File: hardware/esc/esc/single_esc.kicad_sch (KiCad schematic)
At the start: 43 parts, among them Q1 Q_NMOS, Q2 Q_NMOS, Q3 Q_NMOS, Q4 Q_NMOS, Q5 Q_NMOS, Q6 Q_NMOS, U1 NSG2065Q, U2 AT32F421G8U7

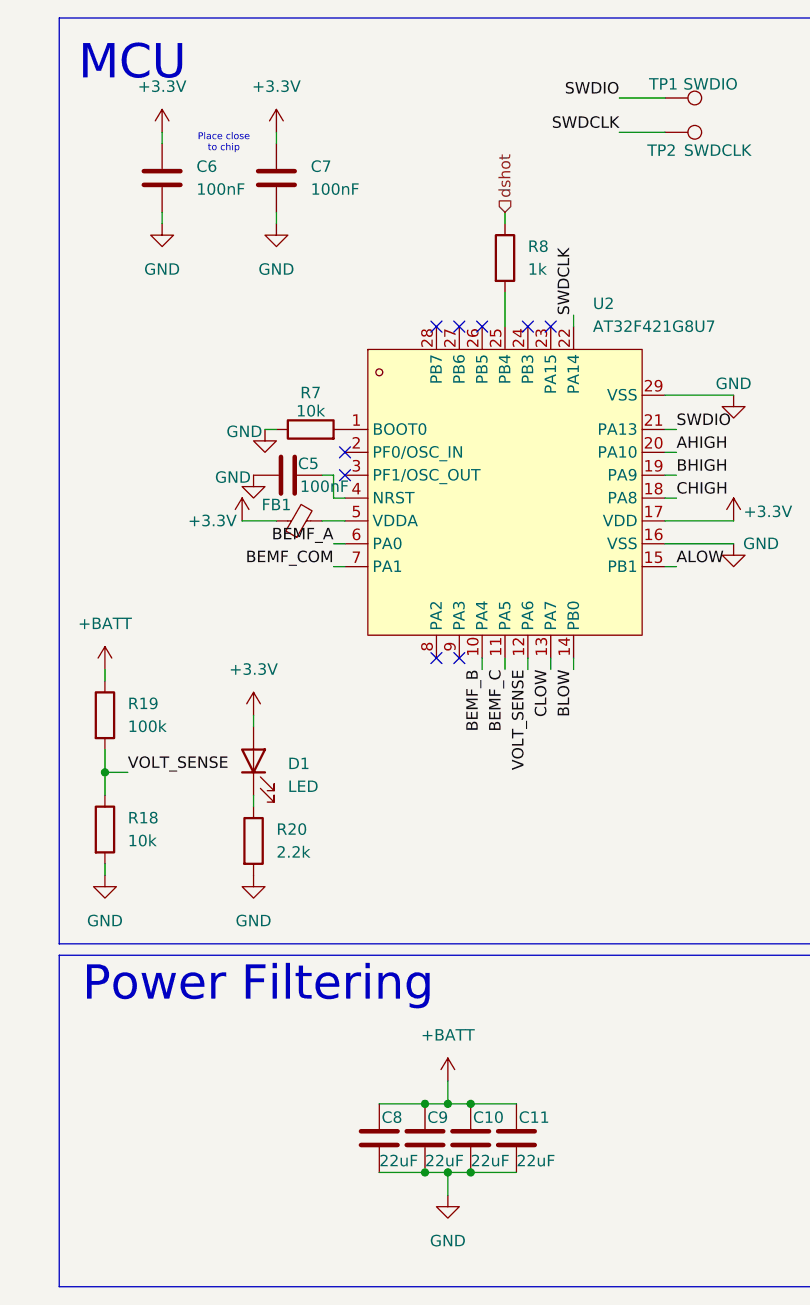
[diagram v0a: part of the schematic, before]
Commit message: redo layout and new board outline
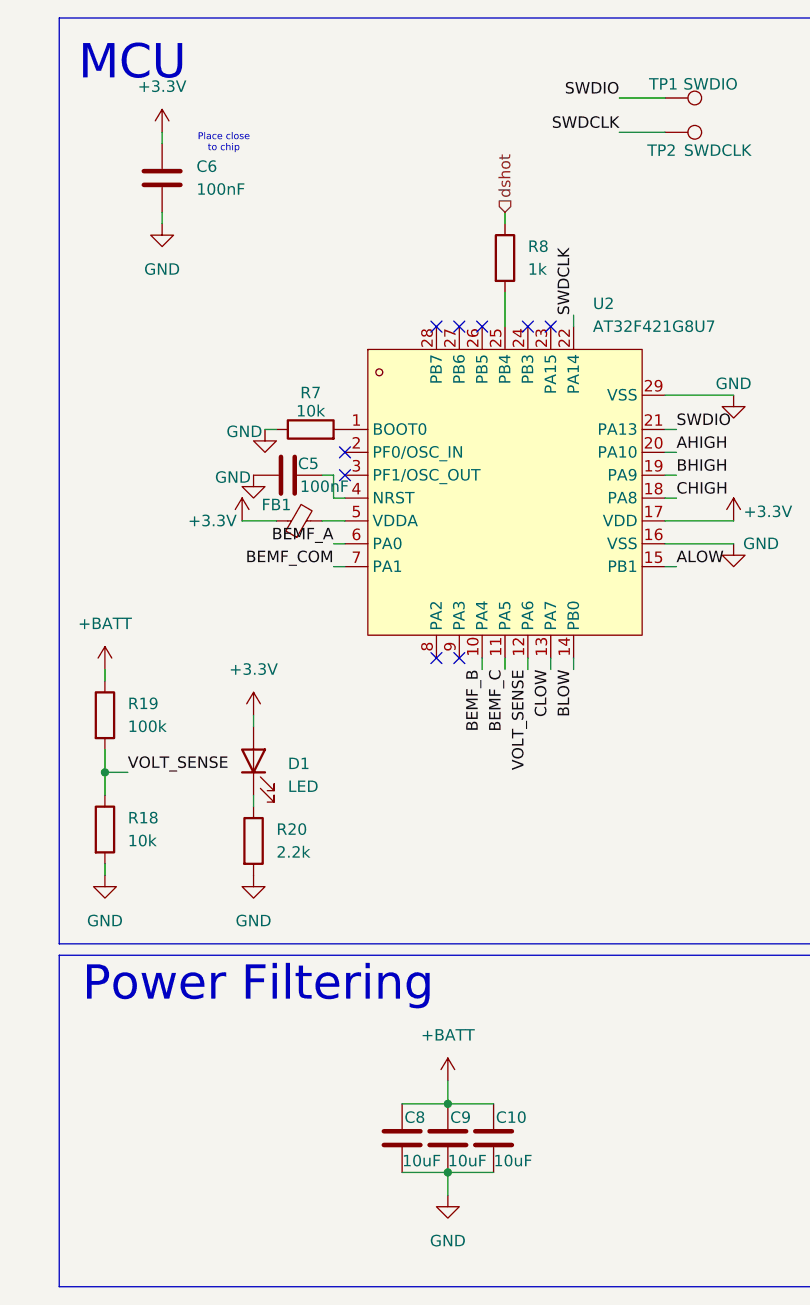
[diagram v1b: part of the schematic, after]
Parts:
- removed C11: 22uF, Capacitor_SMD:C_0805_2012Metric, symbol Device:C
- removed C7: 100nF, Capacitor_SMD:C_0603_1608Metric, symbol Device:C
- C1, C2, C3, C4, C5, C6: footprint Capacitor_SMD:C_0603_1608Metric -> Capacitor_SMD:C_0402_1005Metric
- C10, C8, C9: value 22uF -> 10uF; footprint Capacitor_SMD:C_0805_2012Metric -> Capacitor_SMD:C_0603_1608Metric
- R1, R10, R12, R14, R15, R17, R2, R3, R4, R5, R6, R9: footprint Resistor_SMD:R_0805_2012Metric -> Resistor_SMD:R_0603_1608Metric
- R11, R13, R16: footprint Resistor_SMD:R_0805_2012Metric -> Resistor_SMD:R_0402_1005Metric
- R19: footprint Resistor_SMD:R_0603_1608Metric -> Resistor_SMD:R_0402_1005Metric
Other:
- moved on the sheet: C10, C8, C9
